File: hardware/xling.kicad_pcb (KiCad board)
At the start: 2 copper layers, 35.6 x 48.3 mm, 54 parts, among them J3 MCP73831, J6 Battery, Q1 NTR0202PL, Q2 NTR0202PL, Q3 NTA4153N, SW2 Up, SW3 Select, SW4 Down, U1 LT1109CZ-12, U2 ATMEGA328P-AU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

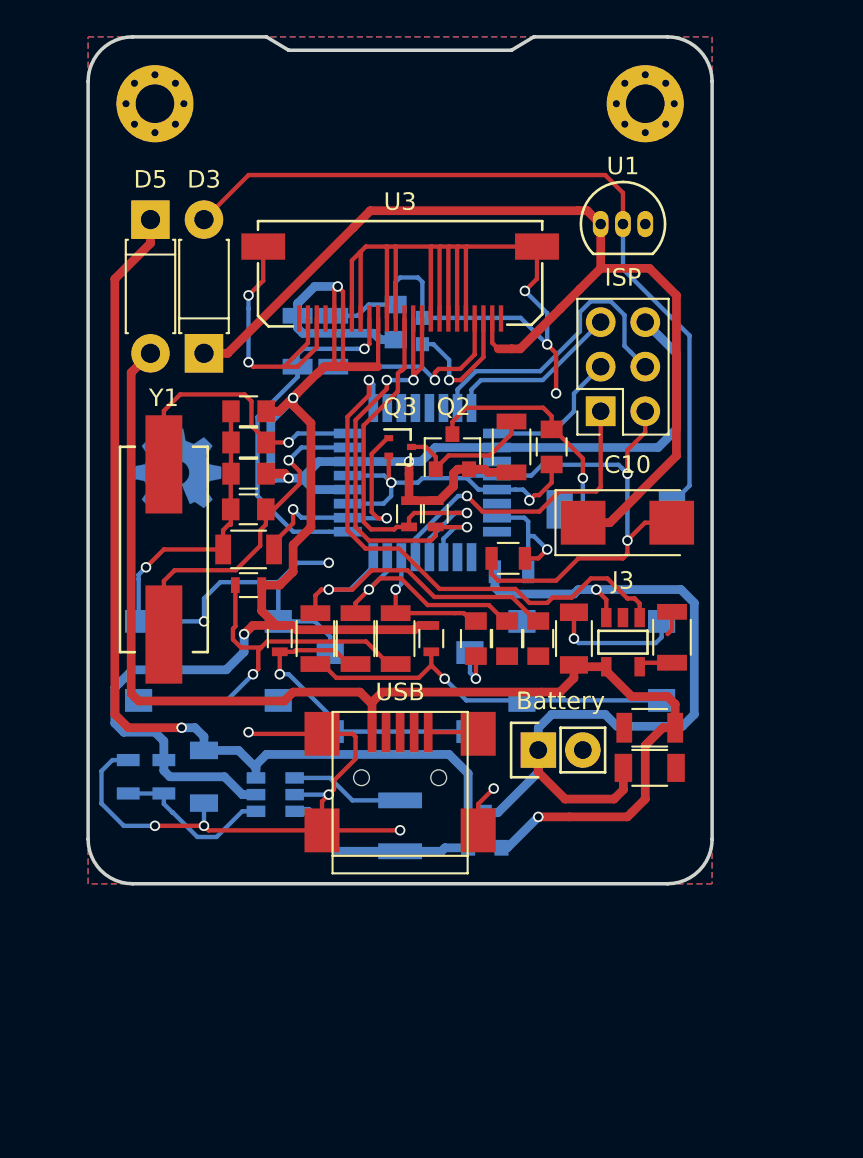
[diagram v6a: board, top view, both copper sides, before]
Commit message: patch 0.2.0002: Update PCB.
Components placed according to their updated footprints. The most
noticible ones are IDC connecter of the AVR ISP and a horizontal battery
connector. There are many minor changes and no routing yet.

Signed-off-by: Dmitry Salychev <darkness.bsd@gmail.com>
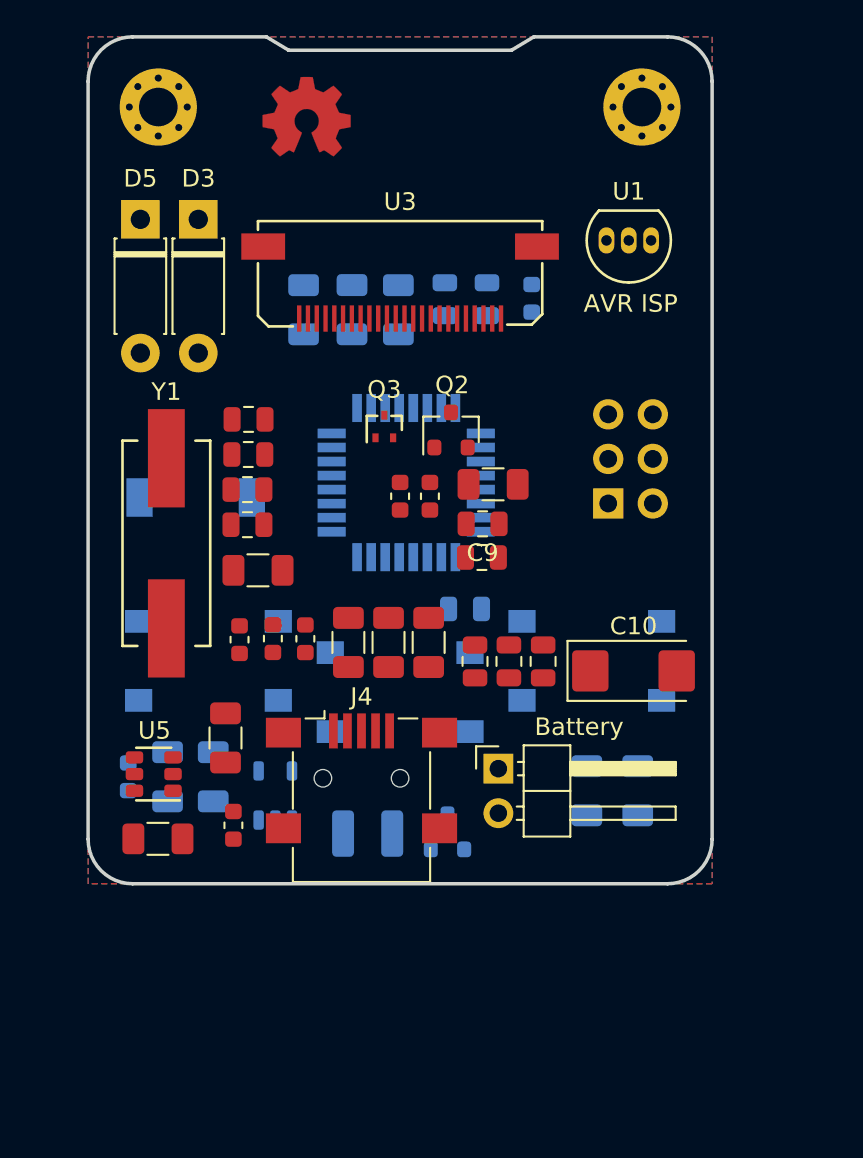
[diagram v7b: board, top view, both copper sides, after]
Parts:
- removed the G*** at (127.0, 100.8)
- removed ISP: AVR ISP, Socket_Strips:Socket_Strip_Straight_2x03_Pitch2.54mm
- removed J3: MCP73831, Xling Footprints:MCP73831_SOT_23
- removed the REF** at (125.7, 80.0)
- removed the REF** at (153.7, 80.0)
- removed USB: USB_OTG, Connectors:USB_Mini-B
- added C2: 4.7uF, Xling Footprints:C_1206_3216Metric, B.Cu at (134.2, 91.8)
- added G***: LOGO, Xling Footprints:oshw, F.Cu at (134.4, 80.8)
- added J4: USB_OTG, Xling Footprints:USB_Mini-B_Lumberg_2486_01_Horizontal, F.Cu at (137.5, 118.5)
- added J5: AVR ISP, Xling Footprints:IDC-Header_2x03_P2.54mm_Vertical, B.Cu at (151.6, 102.8)
- added R13: 100K, Xling Footprints:R_1206_3216Metric, F.Cu at (125.9, 121.9)
- added R20: 110K, Xling Footprints:R_0805_2012Metric, B.Cu at (144.7, 91.2)
- added REF**: MountingHole_2.2mm_M2_Pad_Via, MountingHole:MountingHole_2.2mm_M2_Pad_Via, F.Cu at (125.9, 80.2)
- added REF**: MountingHole_2.2mm_M2_Pad_Via, MountingHole:MountingHole_2.2mm_M2_Pad_Via, F.Cu at (153.5, 80.2)
- added U5: AP3401_TSOT26, Xling Footprints:AP3401_TSOT26, F.Cu at (125.7, 118.2)
- C1: value 10uF -> 22pF; footprint Capacitors_SMD:C_0805 -> Xling Footprints:C_0805_2012Metric
- C10: footprint Capacitors_Tantalum_SMD:CP_Tantalum_Case-C_EIA-6032-28_Reflow -> Xling Footprints:CP_EIA-6032-20_AVX-F
- C11: footprint Capacitors_SMD:C_0603 -> Xling Footprints:C_0603_1608Metric
- C13, C15, C18, C19, C20, C7, C8, C9: footprint Capacitors_SMD:C_0805 -> Xling Footprints:C_0805_2012Metric
- C3, C5: footprint Capacitors_SMD:C_1206 -> Xling Footprints:C_1206_3216Metric
- C6: footprint Capacitors_SMD:C_1206 -> Xling Footprints:C_1206_3216Metric; moved to B.Cu
- D3, D5: footprint Diodes_THT:D_DO-41_SOD81_P7.62mm_Horizontal -> Xling Footprints:D_DO-41_SOD81_P7.62mm_Horizontal
- J6: footprint Xling Footprints:Pin_Header_Straight_1x02 -> Xling Footprints:PinHeader_1x02_P2.54mm_Horizontal
- L1: value 4.7uH -> 2.2uH; footprint Inductors_SMD:L_1210 -> Xling Footprints:L_1210_3225Metric
- L2: footprint Inductors_SMD:L_7.3x7.3_H3.5 -> Xling Footprints:L_7.3x7.3_H3.5
- Q1, Q2: footprint TO_SOT_Packages_SMD:SOT-23 -> Xling Footprints:SOT-23
- R1, R10, R17, R18, R19, R2, R5: footprint Resistors_SMD:R_1206 -> Xling Footprints:R_1206_3216Metric
- R11, R12: footprint Resistors_SMD:R_0805 -> Xling Footprints:R_0805_2012Metric
- R14, R15, R16, R8, R9: footprint Resistors_SMD:R_0603 -> Xling Footprints:R_0603_1608Metric
- R3: value 2K7 -> 4K3; footprint Resistors_SMD:R_1206 -> Xling Footprints:R_0603_1608Metric
- R4: footprint Resistors_SMD:R_1206 -> Xling Footprints:R_1206_3216Metric; moved to B.Cu
- R6: value 191K -> 100K; footprint Resistors_SMD:R_0805 -> Xling Footprints:R_1206_3216Metric
- R7: value 110K -> 510K; footprint Resistors_SMD:R_0805 -> Xling Footprints:R_0603_1608Metric
- SW2: value Up -> BTN; footprint Buttons_Switches_SMD:SW_SPST_PTS645 -> Xling Footprints:SW_SPST_PTS645
- SW3: value Select -> BTN; footprint Buttons_Switches_SMD:SW_SPST_PTS645 -> Xling Footprints:SW_SPST_PTS645
- SW4: value Down -> BTN; footprint Buttons_Switches_SMD:SW_SPST_PTS645 -> Xling Footprints:SW_SPST_PTS645
- U2: footprint Housings_QFP:TQFP-32_7x7mm_Pitch0.8mm -> Xling Footprints:TQFP-32_7x7mm_P0.8mm
- U4: value MCP1640B-CH -> MCP73831; footprint TO_SOT_Packages_SMD:SOT-23-6 -> Xling Footprints:MCP73831_SOT_23
- moved R3 27.2 mm to (130.2, 121.1), turned to 270 degrees
- moved L2 24.0 mm to (128.1, 102.5), turned to 180 degrees
- moved C3 20.6 mm to (129.8, 116.2)
- moved C10 8.45 mm to (153.0, 112.3)
- moved D3 7.64 mm to (128.2, 86.6), turned to 270 degrees
- moved R16 7.18 mm to (134.3, 110.5)
- moved C11 6.50 mm to (147.2, 91.1)
- moved C9 5.89 mm to (144.4, 104.0), turned to 180 degrees
- moved R4 5.07 mm to (150.3, 119.2), turned to 90 degrees
- moved C7 4.46 mm to (131.0, 102.0)
- moved R2 4.12 mm to (139.6, 91.8)
- moved R1 3.58 mm to (137.0, 91.7)
- moved R11 3.39 mm to (143.4, 108.8)
- moved R14 3.15 mm to (130.6, 110.5), turned to 270 degrees
- moved C13 3.12 mm to (131.0, 100.0)
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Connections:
- C1 pad 2: GND -> Net-(C1-Pad2)
- L1 pad 1: Net-(C5-Pad1) -> Net-(L1-Pad1)
- L1 pad 2: Net-(L1-Pad2) -> +3V3
- R3 pad 1: Net-(J3-Pad5) -> Net-(R3-Pad1)
- R6 pad 1: +3V3 -> Net-(R6-Pad1)
- R6 pad 2: Net-(R6-Pad2) -> Net-(C5-Pad1)
- R7 pad 1: Net-(R6-Pad2) -> Net-(C1-Pad2)
- R7 pad 2: GND -> +3V3
- U4 pad 1: Net-(L1-Pad2) -> /BAT_STAT
- U4 pad 3: Net-(C5-Pad1) -> Net-(C6-Pad1)
- U4 pad 4: Net-(R6-Pad2) -> Net-(C3-Pad1)
- U4 pad 5: +3V3 -> Net-(R3-Pad1)
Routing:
- net GND: track 229.6 -> 0.25 mm, vias 20 -> 0
- net +3V3: track 128.6 -> 0.20 mm, vias 5 -> 0
- net Net-(C3-Pad1): track 71.4 -> 0.00 mm, vias 1 -> 0
- net Net-(C5-Pad1): track 67.9 -> 0.00 mm, vias 1 -> 0
- net +12V: track 59.4 -> 0.00 mm
- net Net-(D3-Pad2): track 45.7 -> 0.00 mm
- net Net-(C6-Pad1): track 45.5 -> 0.00 mm, vias 1 -> 0
- net /BAT_STAT: track 31.1 -> 0.00 mm, vias 1 -> 0
- net /OLED_SDA: track 27.6 -> 0.00 mm, vias 3 -> 0
- net Net-(R14-Pad2): track 25.9 -> 0.33 mm, vias 1 -> 0
- net /OLED_SCL: track 23.1 -> 0.00 mm, vias 1 -> 0
- net Net-(R16-Pad2): track 21.9 -> 0.00 mm, vias 1 -> 0
- net /OLED_RES: track 20.8 -> 0.00 mm, vias 1 -> 0
- net Net-(C13-Pad1): track 19.5 -> 0.00 mm, vias 1 -> 0
- net /BTN3: track 19.1 -> 0.12 mm, vias 1 -> 0
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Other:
- board text added: "Xling 0.2.0002 MCUSim.org 03.11.2018"
- board text removed: "(mcusim.org)"
- board text removed: "0.1.22"
- board text removed: "Xling Virtual Monster by MCUSim"

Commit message: patch 0.2.0003: Updated PCB.
This is an updated version of PCB which is almost ready for production.
It contains new footprints for AVR ISP connector, a battery connector and
an MCUSim logo.

There are also many GND vias generated using a python plugin from
https://github.com/jsreynaud/kicad-action-scripts.

Signed-off-by: Dmitry Salychev <darkness.bsd@gmail.com>
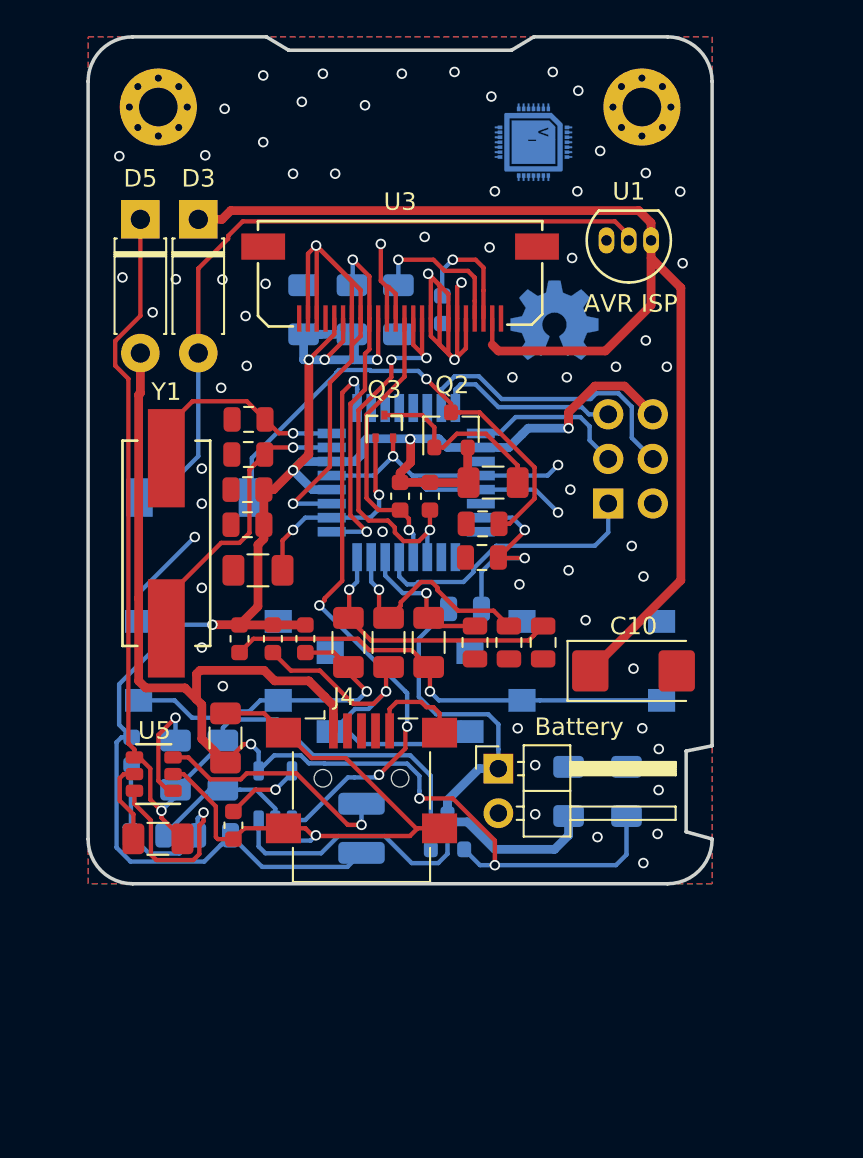
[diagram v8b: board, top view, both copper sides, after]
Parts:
- added G***: LOGO, Xling Footprints:mcusim, B.Cu at (147.3, 82.2)
- G***: moved to B.Cu
- moved R20 36.2 mm to (125.3, 121.7), turned to 180 degrees
- moved C1 33.3 mm to (129.1, 121.7), turned to 180 degrees
- moved SW2 21.8 mm to (150.6, 111.8)
- moved SW4 21.8 mm to (128.8, 111.8)
- moved G*** 18.3 mm to (148.5, 92.4), turned to 180 degrees
- moved C11 5.14 mm to (142.1, 91.8), turned to 270 degrees
- moved C6 3.94 mm to (149.3, 119.2)
- moved R4 2.26 mm to (152.6, 119.2)
- moved R7 1.48 mm to (124.4, 116.9)
- moved C18 1.08 mm to (144.0, 110.7)
- moved C19 1.08 mm to (145.9, 110.7)
- moved C20 1.08 mm to (147.8, 110.7)
- moved C5 0.86 mm to (129.6, 117.7)
- moved R6 0.80 mm to (126.9, 117.7)
- moved L1 0.46 mm to (137.5, 121.3), turned to 270 degrees
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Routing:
- net GND: track 0.25 -> 146.5 mm, vias 0 -> 70
- net +3V3: track 0.20 -> 109.3 mm, vias 0 -> 7
- net Net-(C3-Pad1): track 0.00 -> 72.4 mm, vias 0 -> 3
- net +12V: track 0.00 -> 70.1 mm
- net Net-(C5-Pad1): track 0.00 -> 61.4 mm, vias 0 -> 1
- net Net-(C6-Pad1): track 0.00 -> 43.0 mm
- net Net-(D3-Pad2): track 0.00 -> 41.4 mm
- net /BAT_STAT: track 0.00 -> 33.7 mm, vias 0 -> 4
- net /OLED_VCC: track 0.00 -> 27.5 mm, vias 0 -> 1
- net Net-(R14-Pad2): track 0.33 -> 26.6 mm, vias 0 -> 1
- net /OLED_SDA: track 0.00 -> 24.3 mm, vias 0 -> 3
- net Net-(R15-Pad2): track 0.00 -> 22.8 mm, vias 0 -> 1
- net Net-(C1-Pad2): track 0.00 -> 20.3 mm, vias 0 -> 1
- net /OLED_RES: track 0.00 -> 20.2 mm, vias 0 -> 2
- net Net-(R16-Pad2): track 0.00 -> 18.7 mm, vias 0 -> 1
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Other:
- outline, holes or cut-outs redrawn
- board text added: "Xling 0.2.0003 MCUSim.org"
- board text removed: "Xling 0.2.0002 MCUSim.org 03.11.2018"
